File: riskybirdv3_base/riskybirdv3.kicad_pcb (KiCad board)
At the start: 4 copper layers, 53 x 69.8 mm, 180 parts, among them IC1 PMW3901MB-TXQT, J1 Conn_02x10_Odd_Even, J10 Conn_01x05, J11 Conn_01x05, J2 Conn_01x05, J3 Conn_01x02, J4 Conn_01x02, J5 Conn_01x02, J6 Conn_01x02, J7 Conn_01x02, J8 USB_C_Receptacle_USB2.0_16P, J9 Conn_01x05, Q1 SI2302, Q2 SI2302, Q3 SI2302, Q4 SI2302, Q5 AON7407, Q6 2N7002, Q7 2N7002, SW1 SW_SPST, SW2 SW_SPST, SW4 SW_SPST, SW5 SW_SPST, U1 ADS7128IRTER, U10 TLV70018DCKR, U11 TLV70015DCKT, U12 PCA9306DC, U14 ESP32-C6-MINI-1/U, U2 LTC3119EUFD#TRPBF, U3 BMI088, U4 MCP73831-2-OT, U6 USBLC6-2P6, U7 TLV70028DCKR, U8 TPS2117DRLR_C22399676, U9 VL53L1CXV0FY1

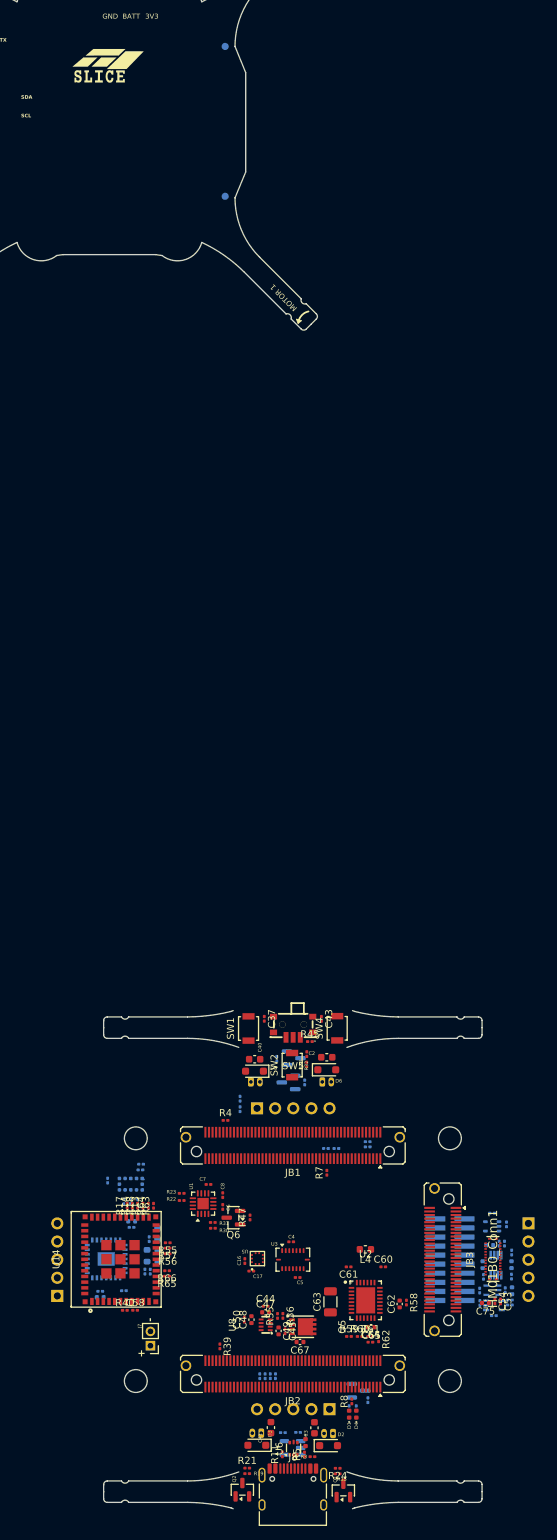
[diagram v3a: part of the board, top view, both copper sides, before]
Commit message: riskybirdv3: route power/signal nets — USB diff-pair swap, buck-boost bottom-layer zones, battery→motor power, GND/3V3 pours; all nets connected
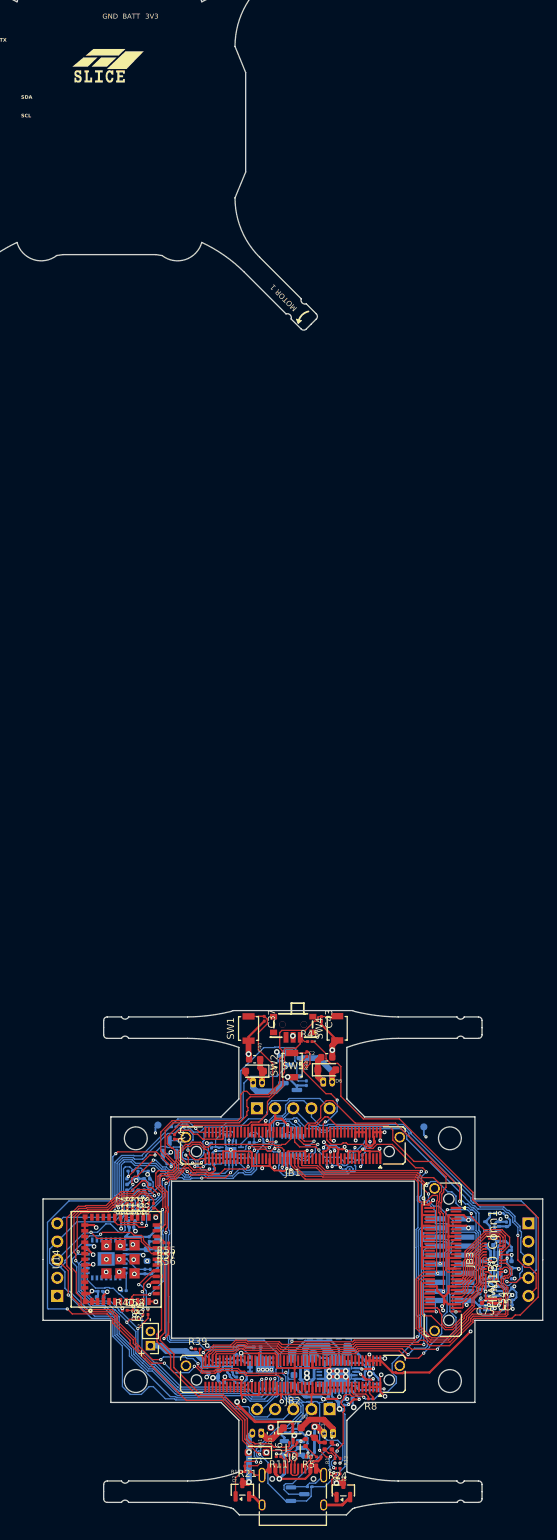
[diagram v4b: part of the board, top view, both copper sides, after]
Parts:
- added R70: 0R, Resistor_SMD:R_1206_3216Metric, B.Cu at (101.4, 113.5)
- C16, C17, C4, C44, C45, C47, C48, C49, C5, C50, C6, C60, C61, C62, C63, C64, C65, C67, C7, C8, L4, Q5, Q6, R22, R23, R30, R31, R35, R36, R47, R58, R59, R60, R61, R62, R7, U1, U2, U3, U5, U8: moved to B.Cu
- R1, R12: moved to F.Cu
- moved TP6 153.9 mm to (118.3, 81.4)
- moved TP1 130.4 mm to (81.1, 81.2), turned to 90 degrees
- moved C17 22.2 mm to (109.7, 85.7), turned to 90 degrees
- moved C16 21.5 mm to (108.3, 84.8), turned to 180 degrees
- moved L4 20.9 mm to (100.2, 117.0), turned to 90 degrees
- moved C60 20.9 mm to (101.9, 118.9), turned to -90 degrees
- moved U5 18.5 mm to (108.0, 86.6), turned to 90 degrees
- moved R58 17.1 mm to (107.2, 120.7), turned to 90 degrees
- moved Q7 16.8 mm to (100.7, 132.8)
- moved C5 16.1 mm to (99.3, 86.5), turned to 180 degrees
- moved C4 16.0 mm to (100.2, 81.5), turned to 180 degrees
- moved U3 16.0 mm to (100.0, 84.0), turned to 180 degrees
- moved C61 15.8 mm to (100.8, 115.1)
- moved C62 15.0 mm to (107.9, 119.5), turned to 180 degrees
- moved R48 14.6 mm to (102.4, 131.8), turned to 180 degrees
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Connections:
- net Net-(J8-D+-PadA6) renamed /CONN_DP
- net Net-(J8-D--PadA7) renamed /CONN_DN
- JB1 pad 50: /TOF_Int -> /INT_BARO
- JB1 pad 52: /INT_BARO -> /TOF_Int
- JB1 pad 86: /TSI_UART_TX -> unconnected-(JB1-Pin_66-Pad86)
- JB1 pad 91: /TSI_UART_RX -> unconnected-(JB1-Pin_71-Pad91)
- JB1 pad 95: unconnected-(JB1-Pin_75-Pad95) -> /U0TXD
- JB1 pad 97: unconnected-(JB1-Pin_77-Pad97) -> /U0RXD
- JB2 pad 25: /TRIG -> unconnected-(JB2-Pin_25-Pad25)
- JB2 pad 27: /INT -> unconnected-(JB2-Pin_27-Pad27)
- JB2 pad 31: /FVLD -> unconnected-(JB2-Pin_31-Pad31)
- JB2 pad 33: /MCLK -> unconnected-(JB2-Pin_33-Pad33)
- JB2 pad 35: /LVLD -> unconnected-(JB2-Pin_35-Pad35)
- JB2 pad 37: /PCLK -> unconnected-(JB2-Pin_37-Pad37)
- JB2 pad 41: /D0 -> unconnected-(JB2-Pin_41-Pad41)
- JB2 pad 43: /D1 -> unconnected-(JB2-Pin_43-Pad43)
- JB2 pad 45: /D2 -> unconnected-(JB2-Pin_45-Pad45)
- JB2 pad 47: /D3 -> unconnected-(JB2-Pin_47-Pad47)
- JB2 pad 51: /D4 -> unconnected-(JB2-Pin_51-Pad51)
- JB2 pad 53: /D5 -> unconnected-(JB2-Pin_53-Pad53)
- JB2 pad 55: /D6 -> unconnected-(JB2-Pin_55-Pad55)
- JB2 pad 57: /D7 -> unconnected-(JB2-Pin_57-Pad57)
- JB3 pad 37: unconnected-(JB3-Pin_37-Pad37) -> /D0
- JB3 pad 38: unconnected-(JB3-Pin_38-Pad38) -> /INT
- JB3 pad 39: unconnected-(JB3-Pin_39-Pad39) -> /D2
- JB3 pad 40: unconnected-(JB3-Pin_40-Pad40) -> /FVLD
- JB3 pad 41: unconnected-(JB3-Pin_41-Pad41) -> /D4
- JB3 pad 42: unconnected-(JB3-Pin_42-Pad42) -> /TRIG
- JB3 pad 43: unconnected-(JB3-Pin_43-Pad43) -> /D6
- JB3 pad 44: unconnected-(JB3-Pin_44-Pad44) -> /LVLD
- JB3 pad 47: unconnected-(JB3-Pin_47-Pad47) -> /D7
- JB3 pad 49: unconnected-(JB3-Pin_49-Pad49) -> /D5
- JB3 pad 51: unconnected-(JB3-Pin_51-Pad51) -> /D3
- JB3 pad 53: unconnected-(JB3-Pin_53-Pad53) -> /D1
- JB3 pad 57: unconnected-(JB3-Pin_57-Pad57) -> /PCLK
- JB3 pad 58: unconnected-(JB3-Pin_58-Pad58) -> /MCLK
- JB3 pad 59: unconnected-(JB3-Pin_59-Pad59) -> /TSI_UART_TX
- JB3 pad 60: unconnected-(JB3-Pin_60-Pad60) -> /TSI_UART_RX
- R27 pad 2: /SCLK -> /NCS
- R29 pad 2: /MOSI -> /SCLK
- R34 pad 2: /NCS -> /MOSI
- U2 pad 2: Net-(C61-Pad2) -> Net-(R70-Pad2)
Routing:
- net GND: track 0.00 -> 369.5 mm, vias 0 -> 80
- net /SDA: track 0.00 -> 200.8 mm, vias 0 -> 7
- net /SCL: track 0.00 -> 192.3 mm, vias 0 -> 3
- net +BATT: track 0.00 -> 161.1 mm, vias 0 -> 6
- net +3V3: track 0.00 -> 146.0 mm, vias 0 -> 37
- net VCOM: track 0.00 -> 143.3 mm, vias 0 -> 10
- net Net-(C45-Pad1): track 0.00 -> 116.7 mm, vias 0 -> 1
- net +1V8: track 0.00 -> 92.7 mm, vias 0 -> 5
- net /MOTOR2: track 0.00 -> 92.1 mm, vias 0 -> 6
- net /MOTOR1: track 0.00 -> 90.0 mm, vias 0 -> 8
- net Net-(JB1-Pin_35): track 0.00 -> 83.0 mm, vias 0 -> 4
- net Net-(Q5-G): track 0.00 -> 75.3 mm, vias 0 -> 1
- net Net-(JB1-Pin_32): track 0.00 -> 70.5 mm, vias 0 -> 4
- net /CHIP_EN: track 0.00 -> 67.8 mm, vias 0 -> 2
- net /GPIO2: track 0.00 -> 66.2 mm, vias 0 -> 3
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- added copper zone on In2.Cu, net +3V3
- added copper zone on In1.Cu, net GND
- added copper zone on B.Cu, net Net-(C60-Pad2)
- added copper zone on B.Cu, net Net-(C61-Pad2)
- added copper zone on B.Cu, net Net-(U2-BST1)
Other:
- board size 53 x 69.8 mm -> 70 x 70.6 mm

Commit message: riskybirdv3: import JLC-accurate DRU, enlarge sub-0.2mm via drills to 0.2mm, relax annular floor to 0.1mm
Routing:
- net VCOM: track 143.3 -> 145.3 mm
- added copper zone on B.Cu, net GND
- added copper zone on F.Cu, net GND

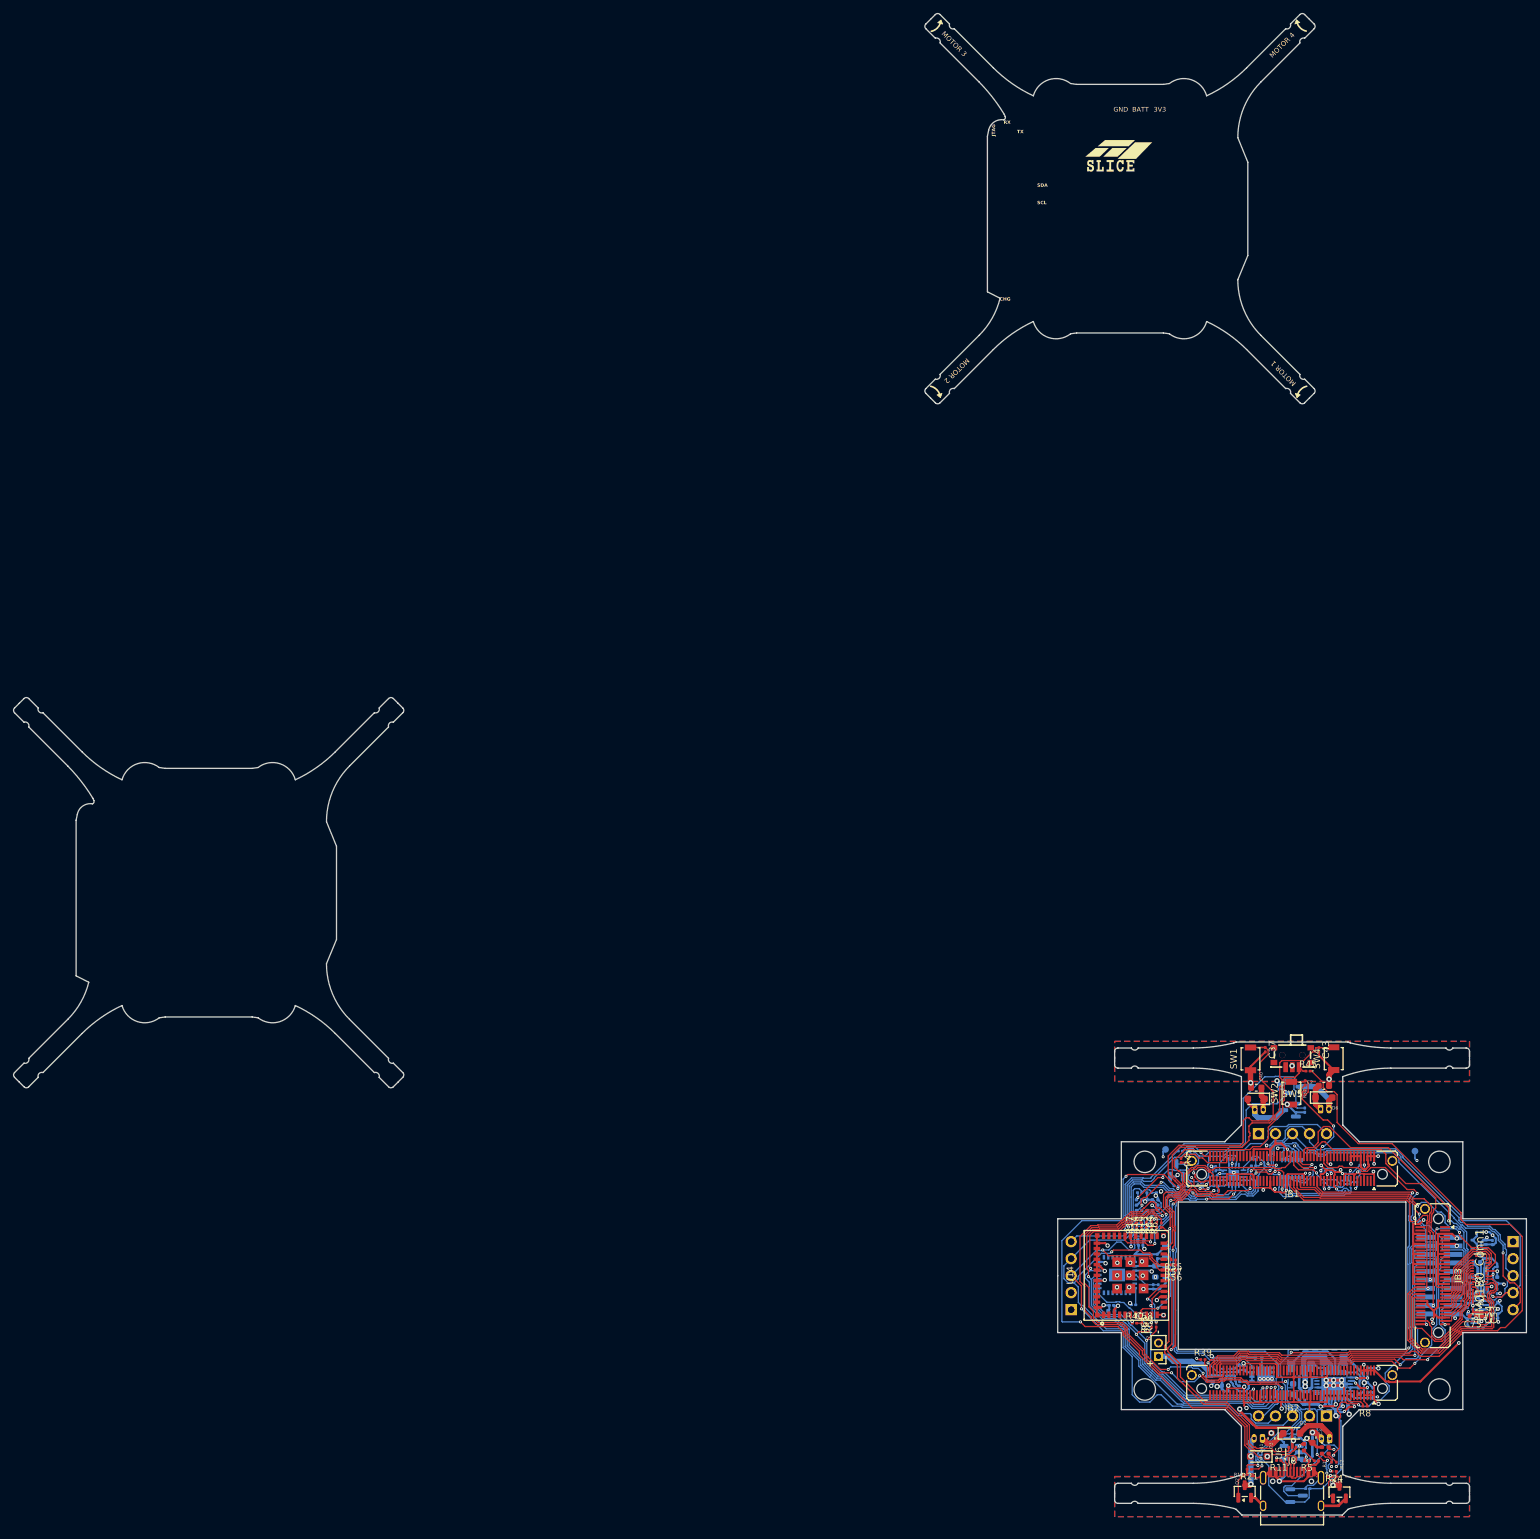
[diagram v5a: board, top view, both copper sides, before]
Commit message: riskybirdv3: ideal-diode ORing power front-end + via provisioning
- Replace undersized TPS2117 mux with ideal-diode OR: LM66100 (USB leg,
  integrated) + LM74700/AON7534 (battery leg, 7A external FET) -> /VSYS
- Add LTC3119 RUN UVLO divider (~3.13V) for 1S over-discharge protection
- VCOM 0.4mm via clusters (Q5<->buck-boost); +3V3 output via stitching (9 vias)
- SW5 mounting pegs -> NPTH; reference designators -> 0.5mm silk
- Import AON7534 (C115844); JLC-accurate DRU silk limits
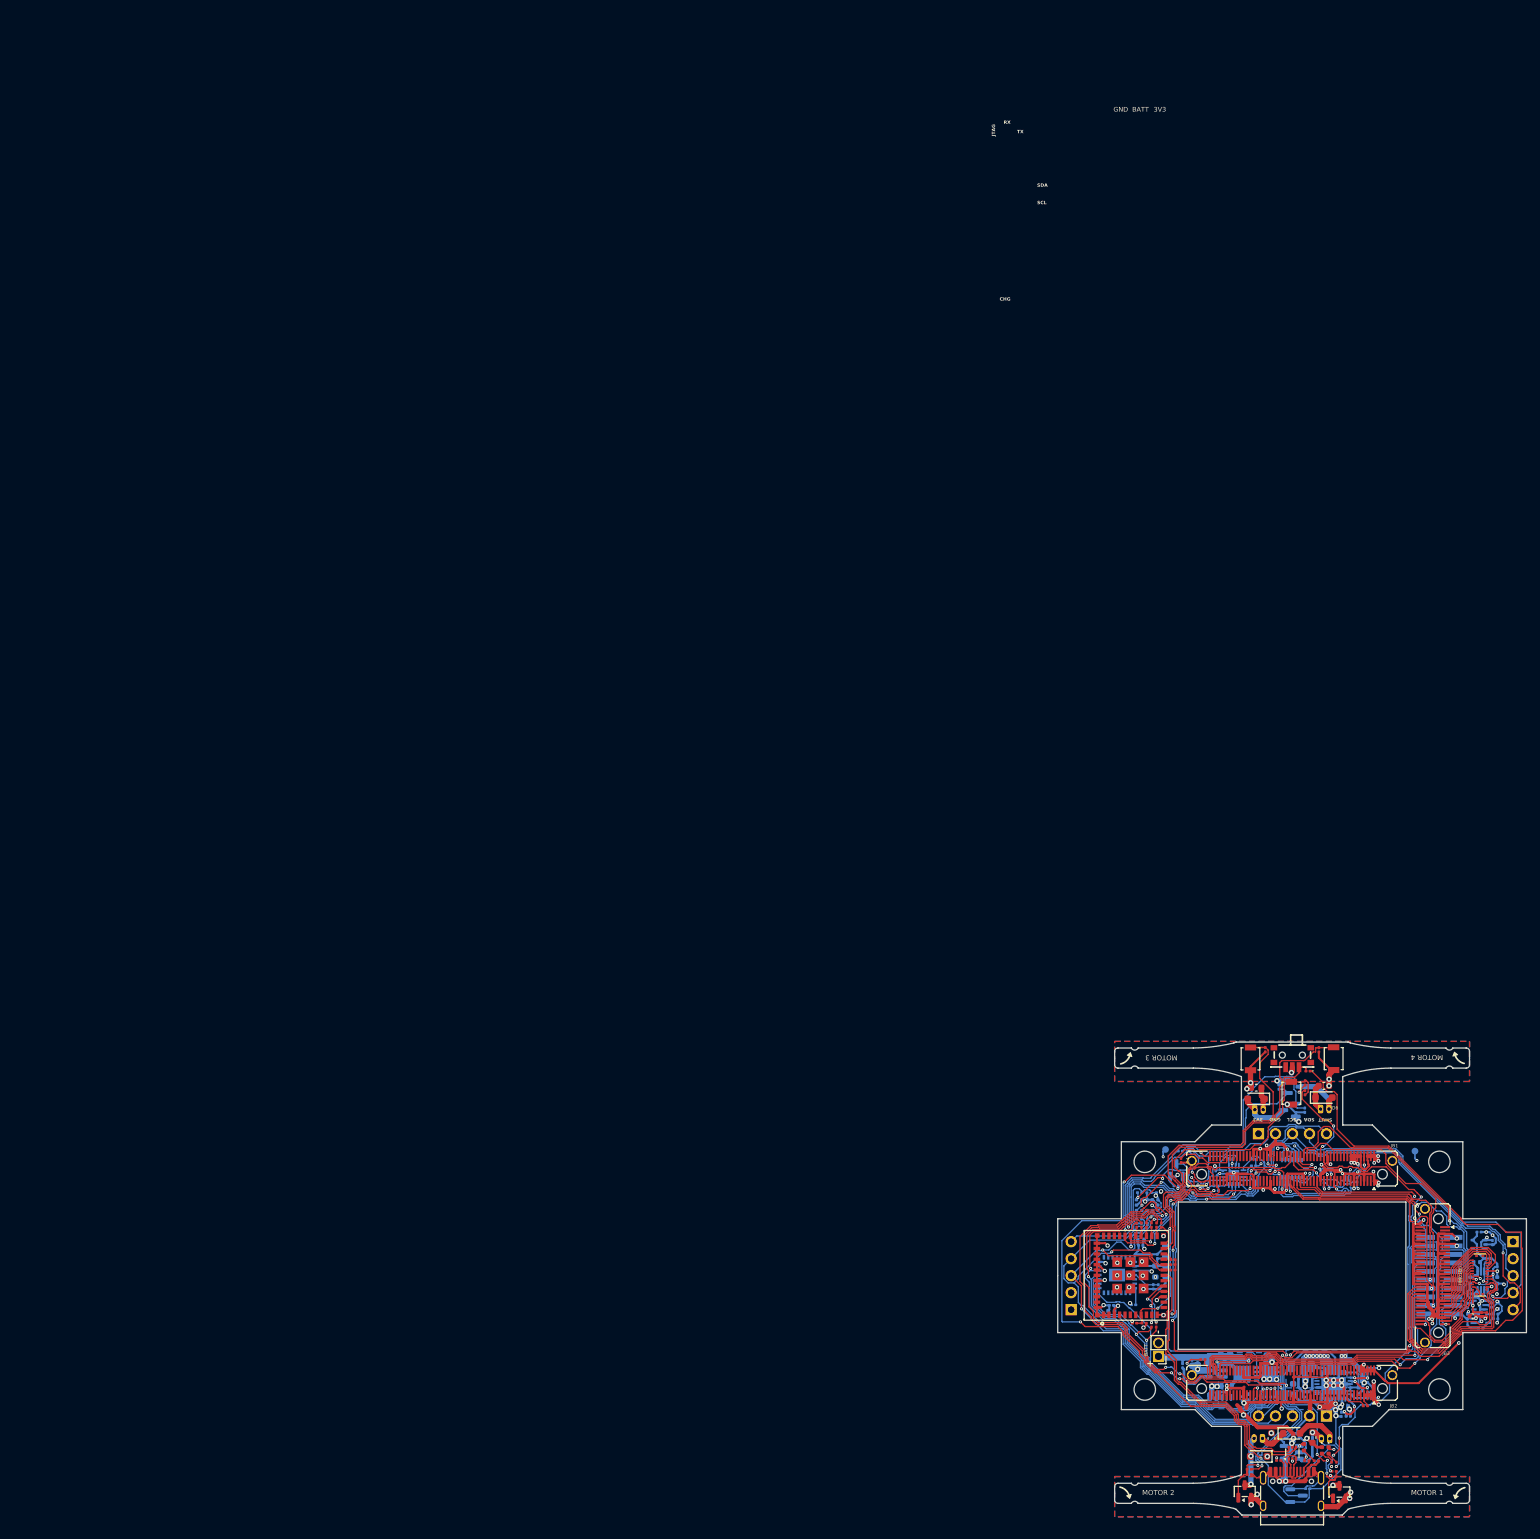
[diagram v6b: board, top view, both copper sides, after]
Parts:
- removed the FID1 at (74.3, -59.4)
- removed the FID1 at (-61.8, 42.8)
- removed R35: 340k, Resistor_SMD:R_0201_0603Metric
- removed R36: 100k, Resistor_SMD:R_0201_0603Metric
- added C77: 0.1u, Capacitor_SMD:C_0201_0603Metric, B.Cu at (83.7, 113.4)
- added Q9: AON7534, riskybird_lcsc:PQFN-8_L3.1-W3.1-P0.65-LS3.3-BL, B.Cu at (92.5, 114.2)
- added R71: 63k, Resistor_SMD:R_0201_0603Metric, B.Cu at (108.4, 121.0)
- added U13: LM74700, Package_TO_SOT_SMD:SOT-23-6, B.Cu at (88.6, 114.2)
- G***: moved to B.Cu
- U8: value TPS2117DRLR_C22399676 -> LM66100DCK; footprint riskybird_lcsc:SOT-583-8_L2.1-W1.2-P0.50-LS1.6-BL -> Package_TO_SOT_SMD:SOT-363_SC-70-6
- moved G*** 186.3 mm to (142.8, 106.0), turned to -90 degrees
- moved G1 180.3 mm to (139.5, 120.5), turned to -135 degrees
- moved G*** 164.9 mm to (118.3, 85.9), turned to 0 degrees
- moved G*** 129.5 mm to (100.0, 68.5), turned to 0 degrees
- moved C45 4.64 mm to (92.6, 118.4), turned to -90 degrees
- moved C49 4.60 mm to (93.5, 118.2), turned to -90 degrees
- moved C48 3.51 mm to (85.9, 112.7)
- moved C50 3.25 mm to (85.0, 113.0)
- moved U8 2.69 mm to (90.2, 117.3)
- moved C47 2.65 mm to (88.2, 118.3)
- moved C44 1.79 mm to (88.4, 117.5)
- moved C67 1.11 mm to (96.1, 112.2), turned to 90 degrees
- moved Q5 0.70 mm to (96.2, 114.7)
- moved C60 0.45 mm to (101.9, 118.5)
- moved R58 0.20 mm to (107.3, 120.7)
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- renumbered TP6 to 3V3, J7 to BATT, TP1 to BATT, G*** to G1, HM01B0_Conn1 to HM01B0
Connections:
- C45 pad 1: Net-(C45-Pad1) -> /VSYS
- C49 pad 1: Net-(C45-Pad1) -> /VSYS
- Q5 pad 1: Net-(C45-Pad1) -> /VSYS
- Q5 pad 2: Net-(C45-Pad1) -> /VSYS
- Q5 pad 3: Net-(C45-Pad1) -> /VSYS
- R45 pad 2: Net-(C45-Pad1) -> /VSYS
- U8 pad 1: GND -> +5V
- U8 pad 2: Net-(C45-Pad1) -> GND
- U8 pad 3: +5V -> /VSYS
- U8 pad 4: Net-(U8-PR1) -> unconnected-(U8-NC-Pad4)
- U8 pad 5: +5V -> unconnected-(U8-ST-Pad5)
- U8 pad 6: +BATT -> /VSYS
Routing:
- net GND: track 369.5 -> 487.3 mm, vias 80 -> 93
- net Net-(C45-Pad1): track 116.7 -> 0.00 mm, vias 1 -> 0
- net /VSYS: track 0.00 -> 109.5 mm, vias 0 -> 1
- net +5V: track 41.0 -> 58.7 mm, vias 4 -> 7
- net VCOM: track 145.3 -> 159.1 mm, vias 10 -> 11
- net +BATT: track 161.1 -> 172.5 mm
- net /D0: track 23.5 -> 14.9 mm, vias 2 -> 0
- net +3V3: track 146.0 -> 153.8 mm, vias 37 -> 47
- net Net-(Q9-G): track 0.00 -> 7.00 mm, vias 0 -> 2
- net /VCAP_BAT: track 0.00 -> 6.15 mm
- net Net-(U8-PR1): track 6.12 -> 0.00 mm
- net /MOTION: track 34.4 -> 38.7 mm
- net /SCL: track 192.3 -> 188.4 mm
- net Net-(R70-Pad2): track 2.89 -> 6.12 mm
- net /GPIO3: track 58.3 -> 61.4 mm, vias 2 -> 4
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- added copper zone on B.Cu, net /VSYS
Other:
- outline, holes or cut-outs redrawn
- board text added: "SHUT"
- board text added: "V3"
- board text removed: "V2"
